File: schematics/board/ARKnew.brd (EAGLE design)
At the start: 82 x 92 mm, 80 parts, among them IC2 STM32F103C8T

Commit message: Схема АРКа + устройства для него
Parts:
- removed S1: (no value), cansat-lib:UNICS-SWITCH
- removed U$3, U$4, U$5: 32961, CanCubeSat:3296W
- added JP4: (no value), pinheadCS:1X02
- added R2: 3313J-1-205E, CanCubeSat:TRIM_3313J-1-205E
- added R4, R5, R6: 3314G-1-504E, CanCubeSat:TRIM_3314G-1-504E
- U$1: value 32961 -> MF-R400; device CanCubeSat:3296W -> CanCubeSat:MF-R400
- moved JP1 277.0 mm to (41.0, 82.4)
- moved JP2 263.5 mm to (79.5, 52.5), turned to 90 degrees
- moved JP3 262.9 mm to (79.5, 45.5), turned to 90 degrees
- moved U$12 123.0 mm to (41.0, 6.00)
- moved IC2 112.5 mm to (66.0, 72.0)
- moved U$1 93.2 mm to (-10.0, -251.0)
- moved C52 82.4 mm to (13.3, 54.6), turned to 270 degrees
- moved R33 81.4 mm to (12.3, 50.6), turned to 180 degrees
- moved LED_G2 80.0 mm to (12.3, 48.1), turned to 90 degrees
- moved R30 77.8 mm to (15.8, 54.6), turned to 90 degrees
- moved C53 76.8 mm to (12.8, 42.1), turned to 270 degrees
- moved C57 74.1 mm to (15.8, 49.6), turned to 90 degrees
- moved R28 70.7 mm to (15.8, 41.1), turned to 90 degrees
- moved C56 69.1 mm to (18.3, 49.1), turned to 90 degrees
- moved C54 69.0 mm to (23.3, 58.6), turned to 270 degrees
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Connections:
- new net GND-OUT: JP1.11, JP1.12, JP2.2, JP3.2, U$1.P$2, U$12.P$3, U$12.P$5, U$12.P$7, U$12.P$9
- net 1.65: now also R4.2, R5.3; no longer U$4.P$2, U$5.P$1
- net 302: now also R5.2; no longer U$5.P$2
- net 3V3: now also R4.1; no longer U$4.P$3
- net A: now also R5.1; no longer U$5.P$3
- net BUS+: now also JP4.2; no longer S1.2
- net BUSPLUS: now also JP4.1; no longer S1.1
- net GND: now also R2.3, R4.3, R6.3; no longer JP1.11, JP1.12, JP2.2, JP3.2, U$12.P$3, U$12.P$5, U$12.P$7, U$12.P$9, U$3.P$1, U$4.P$1
- net INA_BMS+: now also R6.1; no longer U$1.P$3
- net INA_BUS+: now also R2.1; no longer U$3.P$3
- net N$89: now also R6.2; no longer U$1.P$2
- net RUN: now also R2.2; no longer U$3.P$2
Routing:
- net INA_BMS+: track 65.2 -> 16.1 mm
- net Y: track 50.0 -> 28.1 mm, vias 4 -> 3
- net A: track 44.9 -> 25.7 mm
- net PGOOD2: track 37.1 -> 19.9 mm
- net PGOOD1: track 32.7 -> 18.5 mm
- net GND: track 103.7 -> 97.8 mm

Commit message: Доработана схема АРКа
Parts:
- AD5272#2: device CanCubeSat:AD5272 -> CanCubeSat:MSOP10
- C47, C54: device CanCubeSat:ECAP150 -> CanCubeSat:ECAP150-CMD
- C48, C55: device CanCubeSat:ECAP220 -> CanCubeSat:ECAP220-CMD
- INA219#1, U$57: device CanCubeSat:INA219AID -> CanCubeSat:SOT23-8
- INVERT: value INVERTER -> INVERTER.; device CanCubeSat:SOT23-5 -> CanCubeSat:SC70
- moved INA219#1 174.1 mm to (-1.30, -284.1)
- moved AD5272#2 160.1 mm to (-1.00, -300.0)
- moved U$57 159.6 mm to (-1.30, -269.4)
- moved OPA 48.3 mm to (5.60, 47.5)
- moved INVERT 47.4 mm to (5.35, 42.6)
- moved LED_R2 40.4 mm to (5.50, 56.8)
- moved R57 40.4 mm to (5.60, 54.2)
- moved LED_R1 36.5 mm to (6.50, 32.1)
- moved R32 36.5 mm to (6.60, 34.7)
- moved C53 31.1 mm to (13.6, 73.2), turned to 180 degrees
- moved R28 29.3 mm to (12.6, 70.2), turned to 0 degrees
- moved LED_G2 26.6 mm to (19.6, 73.7), turned to 0 degrees
- moved R33 25.1 mm to (22.1, 73.7), turned to 90 degrees
- moved C55 23.4 mm to (13.1, 62.7), turned to 180 degrees
- moved C49 22.9 mm to (12.6, 56.2), turned to 0 degrees
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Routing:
- net INA_BMS+: track 16.1 -> 6.69 mm
- net Y: track 28.1 -> 22.0 mm, vias 3 -> 2
- net GND: track 97.8 -> 95.9 mm, vias 5 -> 4
- net A: track 25.7 -> 24.8 mm
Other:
- board text removed: "3V3"
- board text removed: "GND"

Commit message: Начато исправление разъемов
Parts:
- removed R25, R26: 5k1, resistor:R0603
- JP1: device pinheadCS:2X08 -> pinheadCS:2X09
- moved U$57 356.3 mm to (122.2, 64.8)
- moved INA219#1 356.3 mm to (122.2, 50.1)
- moved U$1 329.9 mm to (59.8, 71.4), turned to 180 degrees
- moved AD5272#2 321.4 mm to (-9.30, 21.3)
- moved R5 290.0 mm to (-21.4, 48.0)
- moved R6 289.1 mm to (-22.5, 35.5)
- moved R4 267.0 mm to (-5.55, 36.3)
- moved R2 254.4 mm to (-4.30, 51.9)
- moved C10 224.3 mm to (120.8, 92.3)
- moved C9 224.3 mm to (115.8, 92.3)
- moved R71 224.3 mm to (117.8, 99.3)
- moved R73 224.3 mm to (125.8, 92.3)
- moved R74 224.3 mm to (115.8, 87.3)
- moved R75 224.3 mm to (125.8, 99.3)
- moved R76 224.3 mm to (120.8, 87.3)
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- renumbered JP2 to CAM1, JP3 to CAM2, JP4 to SWITCH
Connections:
- new net AB-GND: JP1.11, JP1.12
- net 3V3: no longer R25.1, R26.1
- net BMS+: now also JP1.8
- net BUSPLUS: now also JP1.18; no longer JP1.8
- net GND-OUT: now also JP1.13, JP1.14; no longer JP1.11, JP1.12
- net SCLTM: now also JP1.15; no longer JP1.13, R25.2
- net SDATM: now also JP1.16; no longer JP1.14, R26.2
- net TIME: now also JP1.17; no longer JP1.15
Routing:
- net GND: track 95.9 -> 122.4 mm
- net 3V3: track 6.20 -> 28.7 mm
- net SWC: track 0.00 -> 6.97 mm
- net N$161: track 0.00 -> 6.84 mm
- net SCL: track 0.00 -> 6.32 mm
- net NRST: track 0.00 -> 6.20 mm
- net SCLTM: track 0.00 -> 5.88 mm
- net SDA: track 0.00 -> 5.62 mm
- net SDATM: track 0.00 -> 5.39 mm
- net TIME: track 0.00 -> 4.78 mm
- net SWD: track 0.00 -> 4.50 mm
- net I2CINT: track 0.00 -> 4.37 mm
- net N$4: track 0.00 -> 4.26 mm
- net BMS5: track 0.00 -> 3.65 mm
- net N$1: track 0.00 -> 3.36 mm
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
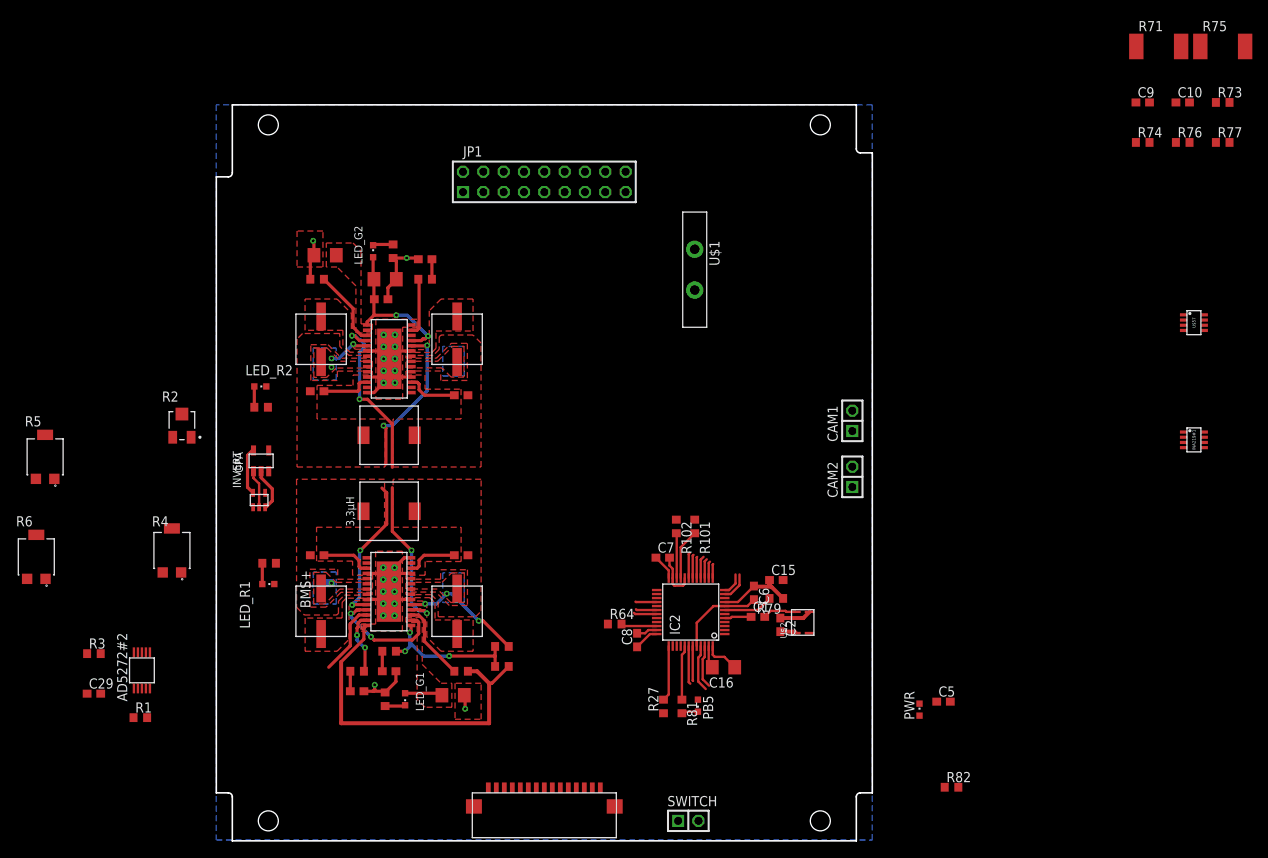
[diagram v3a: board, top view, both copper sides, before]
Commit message: Разведен АРК
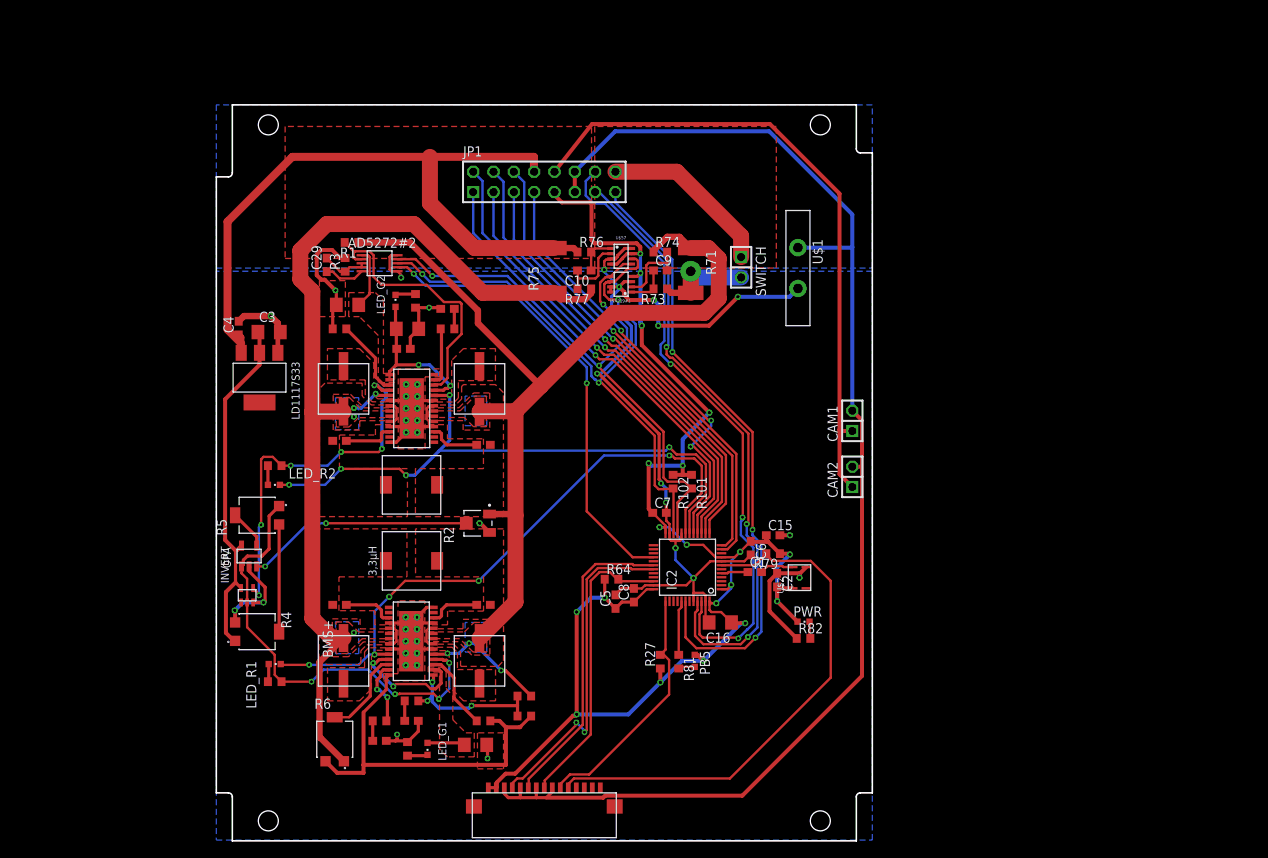
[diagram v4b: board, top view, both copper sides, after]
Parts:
- added C3: 10µ, rcl:C1206
- added C4: 100nF, rcl:C0603
- added LD1117S33: LD1117S33, CanCubeSat:SOT223
- JP1: device pinheadCS:2X09 -> pinheadCS:2X08
- moved R75 88.2 mm to (42.2, 71.3), turned to 90 degrees
- moved R77 81.9 mm to (46.0, 69.0), turned to 180 degrees
- moved C10 77.7 mm to (46.0, 71.3), turned to 180 degrees
- moved R76 76.0 mm to (46.0, 73.6)
- moved INA219#1 74.2 mm to (50.6, 69.6), turned to 180 degrees
- moved R73 74.1 mm to (55.5, 69.0), turned to 180 degrees
- moved U$57 72.1 mm to (50.6, 73.1)
- moved SWITCH 69.5 mm to (65.6, 71.7), turned to 270 degrees
- moved R1 65.0 mm to (16.9, 74.8), turned to 180 degrees
- moved R71 64.9 mm to (59.3, 71.3), turned to 270 degrees
- moved C9 63.9 mm to (55.5, 71.3)
- moved R74 61.8 mm to (55.5, 73.6)
- moved C29 61.0 mm to (13.8, 72.0), turned to 90 degrees
- moved AD5272#2 58.9 mm to (20.4, 72.2), turned to 270 degrees
- moved R3 57.9 mm to (16.1, 72.0), turned to 90 degrees
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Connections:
- removed net AB-GND: JP1.11, JP1.12
- removed net I2CINT: IC2.43
- new net 3V3-STAB: C3.1, INVERT.P$5, LD1117S33.P$3, OPA.P$5, R4.1
- net 3V3: no longer INVERT.P$5, OPA.P$5, R4.1
- net BMS+: now also C4.1, LD1117S33.P$4
- net BMS1: now also IC2.16; no longer IC2.15
- net BMS2: now also IC2.15; no longer IC2.16
- net BMS3: now also IC2.14; no longer IC2.13
- net BMS4: now also IC2.13; no longer IC2.14
- net BMS5: now also IC2.12; no longer IC2.11
- net BMS6: now also IC2.11; no longer IC2.12
- net BUSPLUS: now also JP1.16; no longer JP1.18
- net GND: now also C3.2, C4.2, LD1117S33.P$2
- net GND-OUT: now also JP1.11, JP1.12; no longer JP1.13, JP1.14
- net PGOOD1: now also IC2.19; no longer IC2.18
- net PGOOD2: now also IC2.18; no longer IC2.19
- net SCLTM: now also JP1.13; no longer JP1.15
- net SDATM: now also JP1.14; no longer JP1.16
- net TIME: now also JP1.15; no longer JP1.17
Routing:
- net GND-OUT: track 0.00 -> 165.9 mm
- net 3V3: track 28.7 -> 194.2 mm, vias 0 -> 19
- net GND: track 122.4 -> 261.9 mm, vias 4 -> 21
- net INA_BUS+: track 15.5 -> 131.1 mm
- net INA_BMS+: track 6.69 -> 121.2 mm
- net BMS+: track 0.00 -> 88.6 mm
- net 5V: track 0.00 -> 81.1 mm
- net SDA: track 5.62 -> 79.5 mm, vias 0 -> 3
- net SDATM: track 5.39 -> 79.2 mm, vias 0 -> 3
- net TIME: track 4.78 -> 77.9 mm, vias 0 -> 3
- net SCLTM: track 5.88 -> 77.3 mm, vias 0 -> 3
- net SCL: track 6.32 -> 76.5 mm, vias 0 -> 3
- net NRST: track 6.20 -> 66.6 mm
- net BMS6: track 2.82 -> 59.9 mm, vias 0 -> 1
- net PGOOD1: track 21.4 -> 78.3 mm, vias 2 -> 5
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- added copper zone on layer 1, net BMS+
- added copper zone on layer 1, net BUSPLUS
- added copper zone on layer 16, net GND-OUT
